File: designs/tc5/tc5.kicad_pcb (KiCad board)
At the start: 2 copper layers, 65.4 x 30 mm, 9 parts, among them J1001 Conn_01x04_Male, U1001 MCP6001-OT

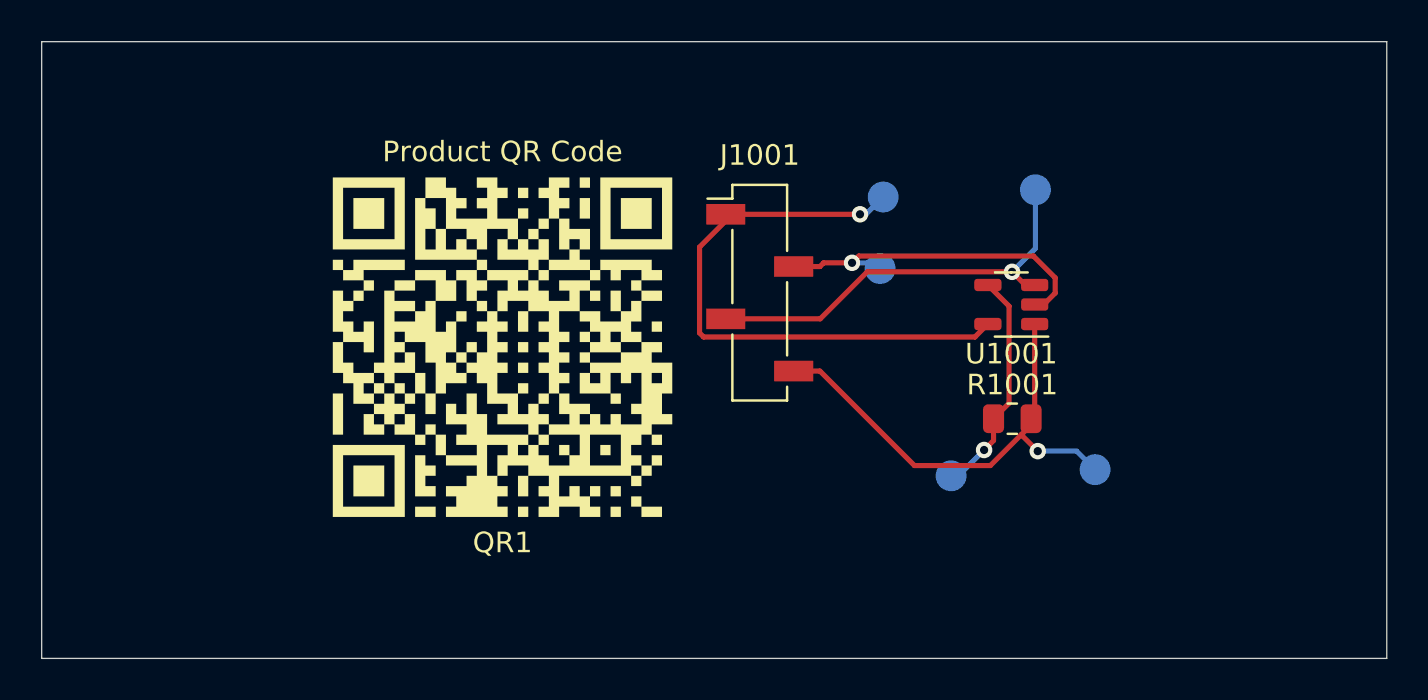
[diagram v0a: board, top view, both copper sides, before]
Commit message: Add component for board edges, generate report
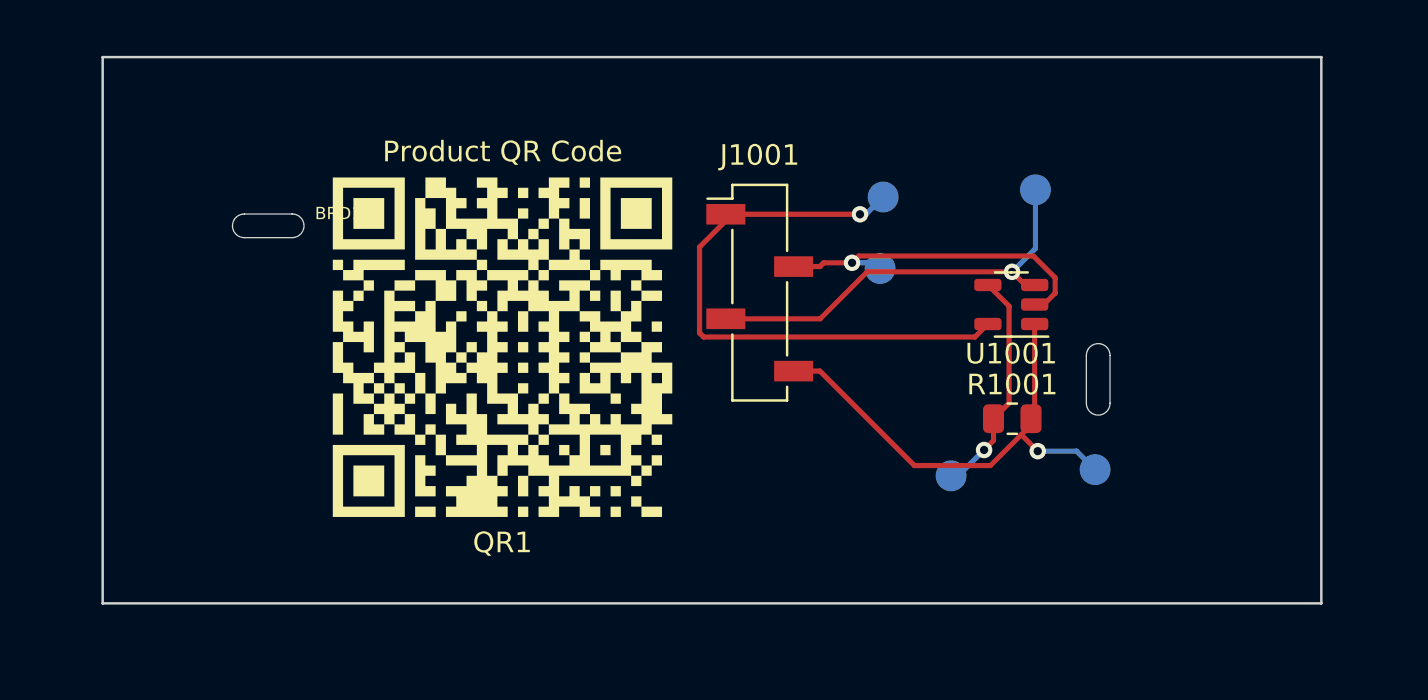
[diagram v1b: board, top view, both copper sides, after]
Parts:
- added BRD1: SYM_Arrow_XLarge, tc5:DemoBoard, F.Cu at (127.3, 91.1)
- J1001: value Conn_01x04_Male -> SSM-104-L-SV
- TP1001: value TP_IN* -> TP_IN
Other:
- board size 65.4 x 30 mm -> 59.2 x 26.5 mm

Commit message: Addec TC2030 for OAR
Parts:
- added P1: TC2030, tc5:TC2030-MCP-FP, F.Cu at (121.5, 98.2)
- added R18: 100k, Resistor_SMD:R_0603_1608Metric, F.Cu at (172.7, 92.5)
- added R59: 100k, Resistor_SMD:R_0603_1608Metric, F.Cu at (168.7, 90.3)
- added R60: 100k, Resistor_SMD:R_0603_1608Metric, F.Cu at (168.7, 93.4)
- added TP1006: TP_HW_TYPE, TestPoint:TestPoint_Pad_D1.5mm, B.Cu at (168.6, 91.9)
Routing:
- net VCC: track 28.8 -> 51.2 mm
- net GND: track 16.8 -> 27.9 mm
- net /V_HW_TYPE: track 0.00 -> 4.29 mm, vias 0 -> 1
- net /OUT: track 23.5 -> 25.9 mm
- net /_AOPIN+: track 11.1 -> 11.8 mm

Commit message: Add resistors to for test
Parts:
- added R20: 330R, Resistor_SMD:R_0805_2012Metric, F.Cu at (168.2, 97.4)
- added R21: 150k, Resistor_SMD:R_0805_2012Metric, F.Cu at (168.2, 99.3)
- added R30: 0R, Resistor_SMD:R_0805_2012Metric, F.Cu at (168.2, 101.2)
- added R31: 0R, Resistor_SMD:R_0805_2012Metric, F.Cu at (168.2, 103.2)
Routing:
- net Net-(R20-Pad1): track 0.00 -> 5.80 mm
- net Net-(R20-Pad2): track 0.00 -> 5.80 mm
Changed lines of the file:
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@@
     (thickness 1.6)
     (drawings 10)
-    (tracks 83)
+    (tracks 87)
     (zones 0)
-    (modules 15)
-    (nets 13)
+    (modules 19)
+    (nets 15)
   )
   (page A4)
@@
   (net 11 "Net-(P1-Pad2)")
   (net 12 "Net-(P1-Pad1)")
+  (net 13 "Net-(R20-Pad2)")
+  (net 14 "Net-(R20-Pad1)")
   (net_class Default "This is the default net class."
     (clearance 0.2)
@@
     (add_net "Net-(P1-Pad5)")
     (add_net "Net-(P1-Pad6)")
+    (add_net "Net-(R20-Pad1)")
+    (add_net "Net-(R20-Pad2)")
     (add_net VCC)
+  )
+  (module Resistor_SMD:R_0805_2012Metric (layer F.Cu)
+    (at 168.21 103.2)
+    (descr "Resistor SMD 0805 (2012 Metric), square (rectangular) end terminal, IPC_7351 nominal, (Body size source: IPC-SM-782 page 72, https://www.pcb-3d.com/wordpress/wp-content/uploads/ipc-sm-782a_amendment_1_and_2.pdf), generated with kicad-footprint-generator")
+    (tags resistor)
+    (attr smd)
+    (fp_text reference R31 (at 3.39 0.2) (layer F.SilkS)
+      (effects (font (size 1 1) (thickness 0.15)))
+    )
+    (fp_text value 0R (at 2.99 0.2) (layer F.Fab) hide
+      (effects (font (size 1 1) (thickness 0.15)))
+    )
+    (fp_line (start 1.68 0.95) (end -1.68 0.95) (layer F.CrtYd) (width 0.05))
+    (fp_line (start 1.68 -0.95) (end 1.68 0.95) (layer F.CrtYd) (width 0.05))
+    (fp_line (start -1.68 -0.95) (end 1.68 -0.95) (layer F.CrtYd) (width 0.05))
+    (fp_line (start -1.68 0.95) (end -1.68 -0.95) (layer F.CrtYd) (width 0.05))
+    (fp_line (start -0.227064 0.735) (end 0.227064 0.735) (layer F.SilkS) (width 0.12))
+    (fp_line (start -0.227064 -0.735) (end 0.227064 -0.735) (layer F.SilkS) (width 0.12))
+    (fp_line (start 1 0.625) (end -1 0.625) (layer F.Fab) (width 0.1))
+    (fp_line (start 1 -0.625) (end 1 0.625) (layer F.Fab) (width 0.1))
+    (fp_line (start -1 -0.625) (end 1 -0.625) (layer F.Fab) (width 0.1))
+    (fp_line (start -1 0.625) (end -1 -0.625) (layer F.Fab) (width 0.1))
+    (fp_text user %R (at 0 0) (layer F.Fab)
+      (effects (font (size 0.5 0.5) (thickness 0.08)))
+    )
+    (pad 2 smd roundrect (at 0.9125 0) (size 1.025 1.4) (layers F.Cu F.Paste F.Mask) (roundrect_rratio 0.243902)
+      (net 13 "Net-(R20-Pad2)"))
+    (pad 1 smd roundrect (at -0.9125 0) (size 1.025 1.4) (layers F.Cu F.Paste F.Mask) (roundrect_rratio 0.243902)
+      (net 14 "Net-(R20-Pad1)"))
+    (model ${KISYS3DMOD}/Resistor_SMD.3dshapes/R_0805_2012Metric.wrl
+      (at (xyz 0 0 0))
+      (scale (xyz 1 1 1))
+      (rotate (xyz 0 0 0))
+    )
+  )
+  (module Resistor_SMD:R_0805_2012Metric (layer F.Cu)
+    (at 168.21 101.2)
+    (descr "Resistor SMD 0805 (2012 Metric), square (rectangular) end terminal, IPC_7351 nominal, (Body size source: IPC-SM-782 page 72, https://www.pcb-3d.com/wordpress/wp-content/uploads/ipc-sm-782a_amendment_1_and_2.pdf), generated with kicad-footprint-generator")
+    (tags resistor)
+    (attr smd)
+    (fp_text reference R30 (at 3.39 0) (layer F.SilkS)
+      (effects (font (size 1 1) (thickness 0.15)))
+    )
+    (fp_text value 0R (at 2.99 0) (layer F.Fab) hide
+      (effects (font (size 1 1) (thickness 0.15)))
+    )
+    (fp_line (start 1.68 0.95) (end -1.68 0.95) (layer F.CrtYd) (width 0.05))
+    (fp_line (start 1.68 -0.95) (end 1.68 0.95) (layer F.CrtYd) (width 0.05))
+    (fp_line (start -1.68 -0.95) (end 1.68 -0.95) (layer F.CrtYd) (width 0.05))
+    (fp_line (start -1.68 0.95) (end -1.68 -0.95) (layer F.CrtYd) (width 0.05))
+    (fp_line (start -0.227064 0.735) (end 0.227064 0.735) (layer F.SilkS) (width 0.12))
+    (fp_line (start -0.227064 -0.735) (end 0.227064 -0.735) (layer F.SilkS) (width 0.12))
+    (fp_line (start 1 0.625) (end -1 0.625) (layer F.Fab) (width 0.1))
+    (fp_line (start 1 -0.625) (end 1 0.625) (layer F.Fab) (width 0.1))
+    (fp_line (start -1 -0.625) (end 1 -0.625) (layer F.Fab) (width 0.1))
+    (fp_line (start -1 0.625) (end -1 -0.625) (layer F.Fab) (width 0.1))
+    (fp_text user %R (at 0 0) (layer F.Fab)
+      (effects (font (size 0.5 0.5) (thickness 0.08)))
+    )
+    (pad 2 smd roundrect (at 0.9125 0) (size 1.025 1.4) (layers F.Cu F.Paste F.Mask) (roundrect_rratio 0.243902)
+      (net 13 "Net-(R20-Pad2)"))
+    (pad 1 smd roundrect (at -0.9125 0) (size 1.025 1.4) (layers F.Cu F.Paste F.Mask) (roundrect_rratio 0.243902)
+      (net 14 "Net-(R20-Pad1)"))
+    (model ${KISYS3DMOD}/Resistor_SMD.3dshapes/R_0805_2012Metric.wrl
+      (at (xyz 0 0 0))
+      (scale (xyz 1 1 1))
+      (rotate (xyz 0 0 0))
+    )
+  )
+  (module Resistor_SMD:R_0805_2012Metric (layer F.Cu)
+    (at 168.2 99.35)
+    (descr "Resistor SMD 0805 (2012 Metric), square (rectangular) end terminal, IPC_7351 nominal, (Body size source: IPC-SM-782 page 72, https://www.pcb-3d.com/wordpress/wp-content/uploads/ipc-sm-782a_amendment_1_and_2.pdf), generated with kicad-footprint-generator")
+    (tags resistor)
+    (attr smd)
+    (fp_text reference R21 (at 3.4 -0.15) (layer F.SilkS)
+      (effects (font (size 1 1) (thickness 0.15)))
+    )
+    (fp_text value 150k (at 3.8 -0.15) (layer F.Fab) hide
+      (effects (font (size 1 1) (thickness 0.15)))
+    )
+    (fp_line (start 1.68 0.95) (end -1.68 0.95) (layer F.CrtYd) (width 0.05))
+    (fp_line (start 1.68 -0.95) (end 1.68 0.95) (layer F.CrtYd) (width 0.05))
+    (fp_line (start -1.68 -0.95) (end 1.68 -0.95) (layer F.CrtYd) (width 0.05))
+    (fp_line (start -1.68 0.95) (end -1.68 -0.95) (layer F.CrtYd) (width 0.05))
+    (fp_line (start -0.227064 0.735) (end 0.227064 0.735) (layer F.SilkS) (width 0.12))
+    (fp_line (start -0.227064 -0.735) (end 0.227064 -0.735) (layer F.SilkS) (width 0.12))
+    (fp_line (start 1 0.625) (end -1 0.625) (layer F.Fab) (width 0.1))
+    (fp_line (start 1 -0.625) (end 1 0.625) (layer F.Fab) (width 0.1))
+    (fp_line (start -1 -0.625) (end 1 -0.625) (layer F.Fab) (width 0.1))
+    (fp_line (start -1 0.625) (end -1 -0.625) (layer F.Fab) (width 0.1))
+    (fp_text user %R (at 0 0) (layer F.Fab)
+      (effects (font (size 0.5 0.5) (thickness 0.08)))
+    )
+    (pad 2 smd roundrect (at 0.9125 0) (size 1.025 1.4) (layers F.Cu F.Paste F.Mask) (roundrect_rratio 0.243902)
+      (net 13 "Net-(R20-Pad2)"))
+    (pad 1 smd roundrect (at -0.9125 0) (size 1.025 1.4) (layers F.Cu F.Paste F.Mask) (roundrect_rratio 0.243902)
+      (net 14 "Net-(R20-Pad1)"))
+    (model ${KISYS3DMOD}/Resistor_SMD.3dshapes/R_0805_2012Metric.wrl
+      (at (xyz 0 0 0))
+      (scale (xyz 1 1 1))
+      (rotate (xyz 0 0 0))
+    )
+  )
+  (module Resistor_SMD:R_0805_2012Metric (layer F.Cu)
+    (at 168.2 97.4)
+    (descr "Resistor SMD 0805 (2012 Metric), square (rectangular) end terminal, IPC_7351 nominal, (Body size source: IPC-SM-782 page 72, https://www.pcb-3d.com/wordpress/wp-content/uploads/ipc-sm-782a_amendment_1_and_2.pdf), generated with kicad-footprint-generator")
+    (tags resistor)
+    (attr smd)
+    (fp_text reference R20 (at 3.4 0) (layer F.SilkS)
+      (effects (font (size 1 1) (thickness 0.15)))
+    )
+    (fp_text value 330R (at 4 0) (layer F.Fab) hide
+      (effects (font (size 1 1) (thickness 0.15)))
+    )
+    (fp_line (start 1.68 0.95) (end -1.68 0.95) (layer F.CrtYd) (width 0.05))
+    (fp_line (start 1.68 -0.95) (end 1.68 0.95) (layer F.CrtYd) (width 0.05))
+    (fp_line (start -1.68 -0.95) (end 1.68 -0.95) (layer F.CrtYd) (width 0.05))
+    (fp_line (start -1.68 0.95) (end -1.68 -0.95) (layer F.CrtYd) (width 0.05))
+    (fp_line (start -0.227064 0.735) (end 0.227064 0.735) (layer F.SilkS) (width 0.12))
+    (fp_line (start -0.227064 -0.735) (end 0.227064 -0.735) (layer F.SilkS) (width 0.12))
+    (fp_line (start 1 0.625) (end -1 0.625) (layer F.Fab) (width 0.1))
+    (fp_line (start 1 -0.625) (end 1 0.625) (layer F.Fab) (width 0.1))
+    (fp_line (start -1 -0.625) (end 1 -0.625) (layer F.Fab) (width 0.1))
+    (fp_line (start -1 0.625) (end -1 -0.625) (layer F.Fab) (width 0.1))
+    (fp_text user %R (at 0 0) (layer F.Fab)
+      (effects (font (size 0.5 0.5) (thickness 0.08)))
+    )
+    (pad 2 smd roundrect (at 0.9125 0) (size 1.025 1.4) (layers F.Cu F.Paste F.Mask) (roundrect_rratio 0.243902)
+      (net 13 "Net-(R20-Pad2)"))
+    (pad 1 smd roundrect (at -0.9125 0) (size 1.025 1.4) (layers F.Cu F.Paste F.Mask) (roundrect_rratio 0.243902)
+      (net 14 "Net-(R20-Pad1)"))
+    (model ${KISYS3DMOD}/Resistor_SMD.3dshapes/R_0805_2012Metric.wrl
+      (at (xyz 0 0 0))
+      (scale (xyz 1 1 1))
+      (rotate (xyz 0 0 0))
+    )
   )
   (module tc5:TC2030-MCP-FP (layer F.Cu)
@@
     (fp_text value TC2030 (at -0.35 -0.6 90) (layer F.Fab)
       (effects (font (size 0.7 0.7) (thickness 0.1)))
-    )
-    (fp_text user %R (at 0.12 0.54 90) (layer F.Fab)
-      (effects (font (size 0.6 0.6) (thickness 0.1)))
     )
     (fp_line (start -0.15 3.45) (end 1.4 3.45) (layer B.CrtYd) (width 0.05))
@@
     (fp_circle (center 0.635 -2.54) (end 2.0725 -2.54) (layer Dwgs.User) (width 0.01))
     (fp_circle (center 0.635 2.54) (end 2.0725 2.54) (layer Dwgs.User) (width 0.01))
+    (fp_text user %R (at 0.12 0.54 90) (layer F.Fab)
+      (effects (font (size 0.6 0.6) (thickness 0.1)))
+    )
     (pad "" np_thru_hole circle (at 0.635 2.54 90) (size 2.3749 2.3749) (drill 2.3749) (layers *.Cu *.Mask F.SilkS))
     (pad "" np_thru_hole circle (at 0.635 -2.54 90) (size 2.3749 2.3749) (drill 2.3749) (layers *.Cu *.Mask F.SilkS))
@@
   (segment (start 169.1759 92.4259) (end 169.983 92.4259) (width 0.25) (layer B.Cu) (net 6))
   (via (at 169.983 92.4259) (size 0.8) (layers F.Cu B.Cu) (net 6))
+  (segment (start 169.1125 103.19) (end 169.1225 103.2) (width 0.25) (layer F.Cu) (net 13))
+  (segment (start 169.1125 97.4) (end 169.1125 103.19) (width 0.25) (layer F.Cu) (net 13))
+  (segment (start 167.2975 97.41) (end 167.2875 97.4) (width 0.25) (layer F.Cu) (net 14))
+  (segment (start 167.2975 103.2) (end 167.2975 97.41) (width 0.25) (layer F.Cu) (net 14))
 )
